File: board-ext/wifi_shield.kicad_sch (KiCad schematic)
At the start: 24 parts, among them J1 Conn_02x05_Counter_Clockwise, J10 Conn_01x01, J11 Conn_01x01, J12 Conn_01x01, J13 Conn_01x01, J14 Conn_01x01, J2 Conn_01x06, J3 Conn_01x04, J4 Conn_01x14, J5 Conn_01x04, J6 Conn_01x14, J7 Conn_01x04, J8 Conn_02x11_Top_Bottom, J9 Conn_01x01, U1 ESP-12E, U2 lowpowerlab_BME280

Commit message: updated design files to kicad7, added GND plane for ext-board v1.3.
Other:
- company: Librelab / SDS / UVA -> librelab

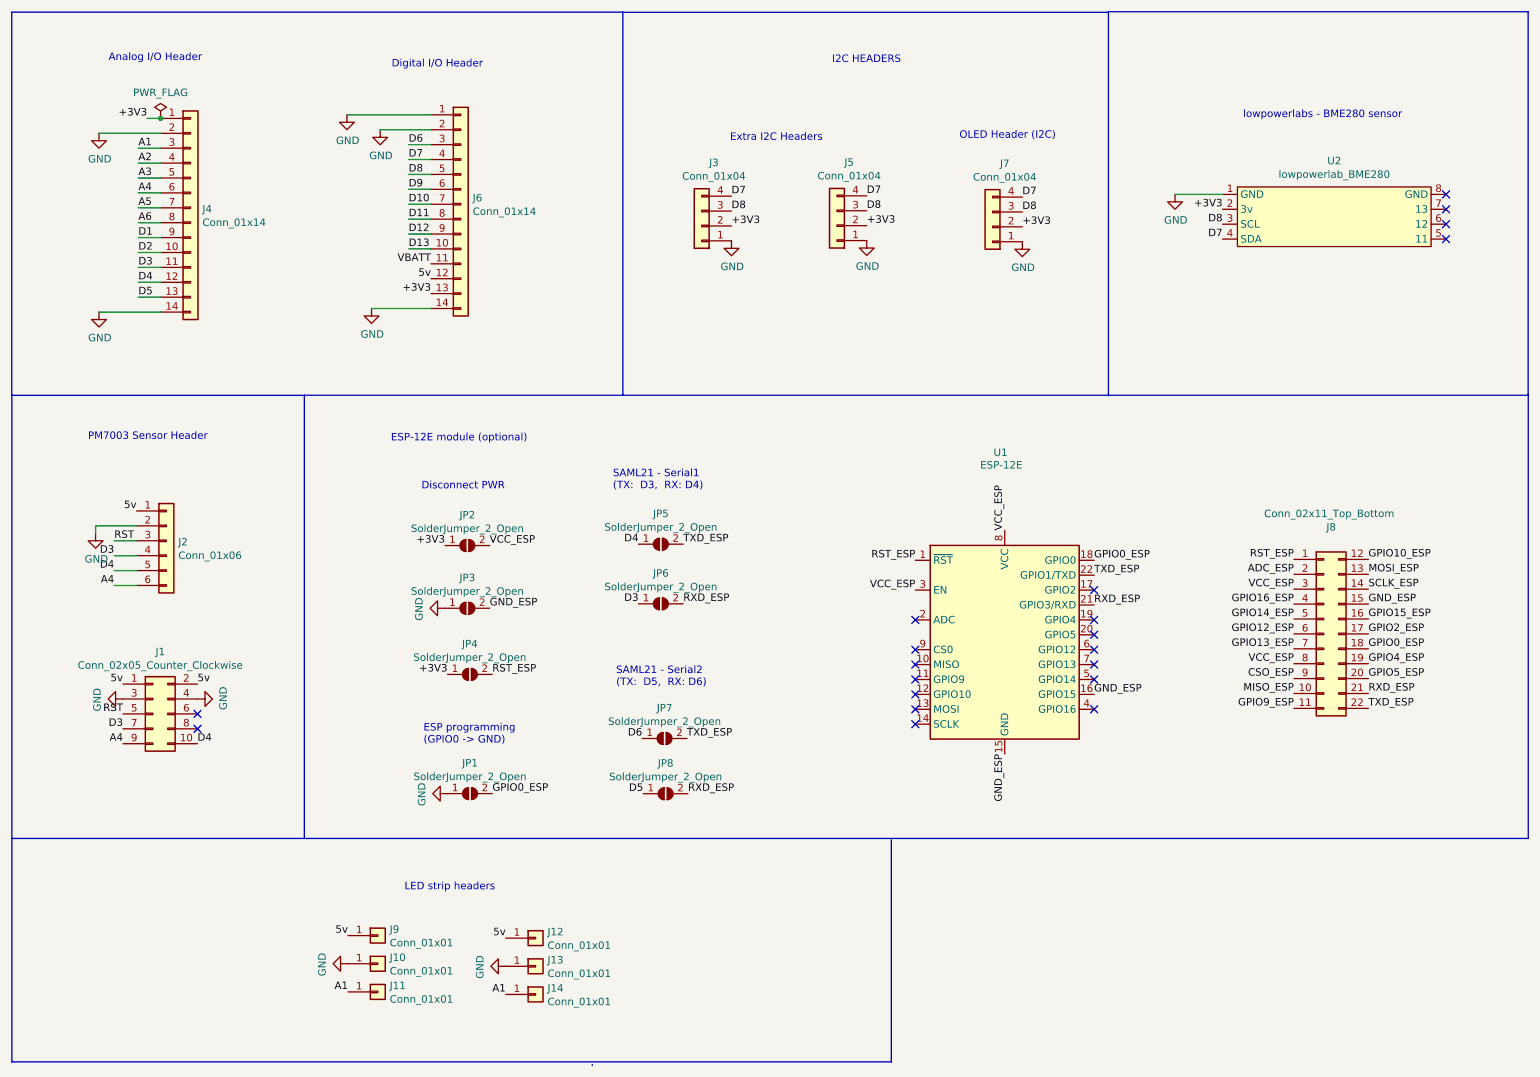
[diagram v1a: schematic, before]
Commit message: added new extension board for Tainã.
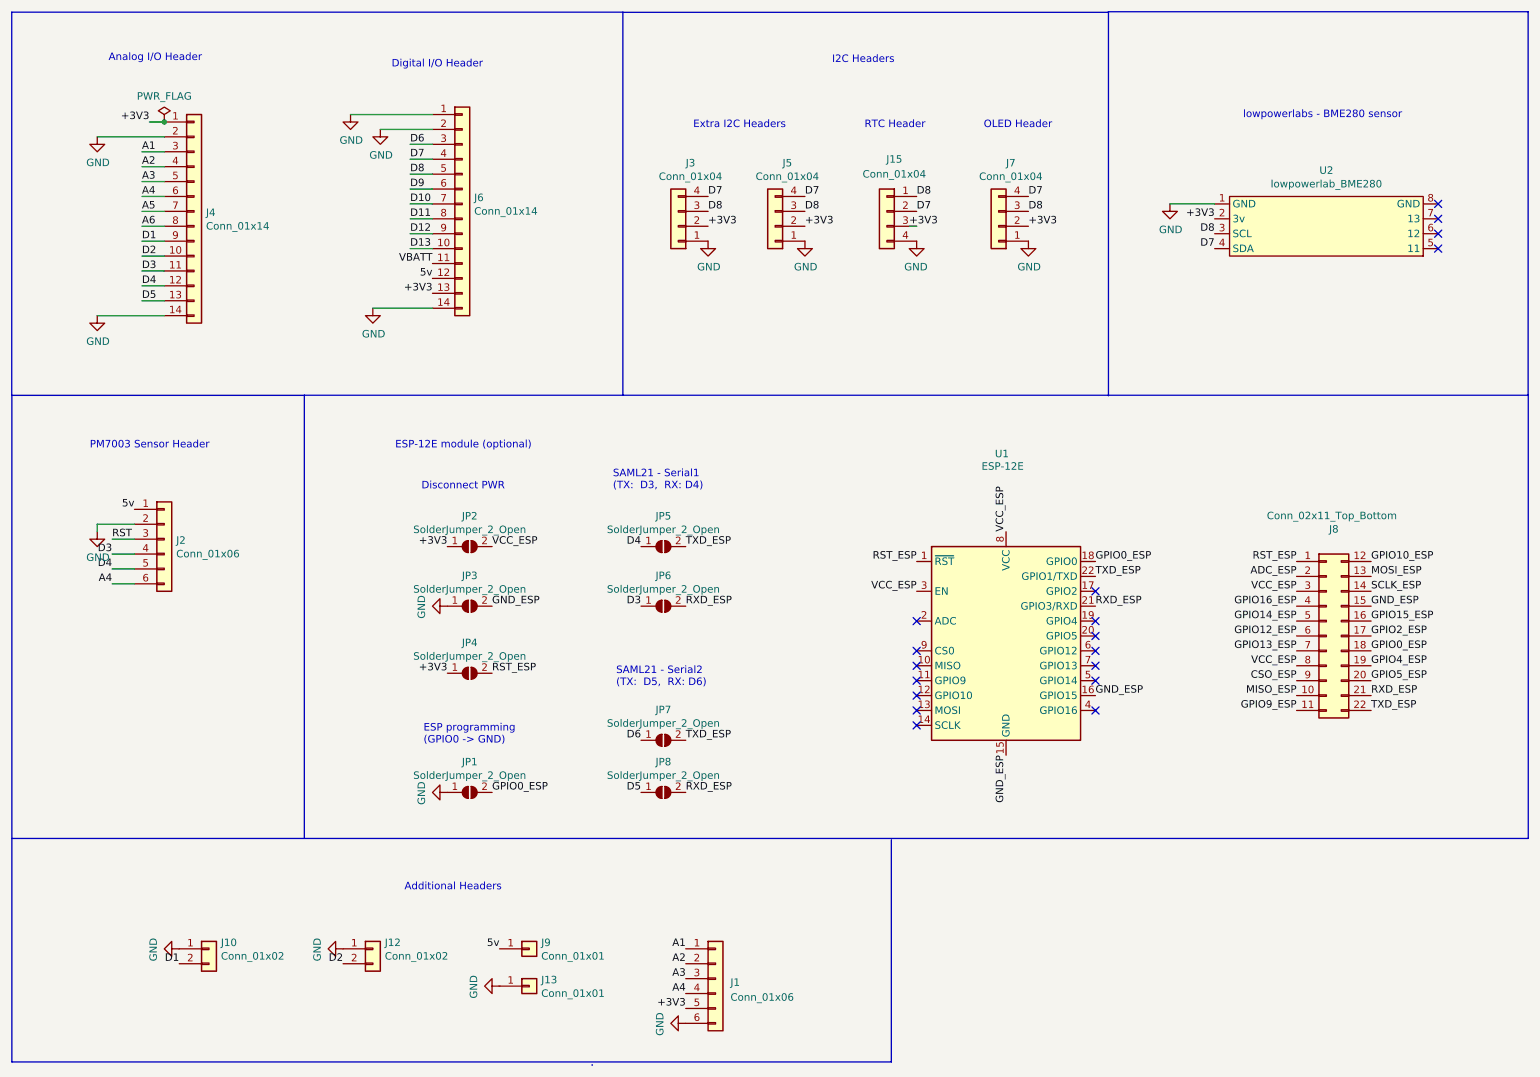
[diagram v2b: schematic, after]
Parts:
- removed J1: Conn_02x05_Counter_Clockwise, Connector_PinHeader_1.27mm:PinHeader_2x05_P1.27mm_Vertical, symbol Connector_Generic:Conn_02x05_Odd_Even
- removed J11, J14: Conn_01x01, Connector_PinHeader_2.54mm:PinHeader_1x01_P2.54mm_Vertical, symbol Connector_Generic:Conn_01x01
- added J1: Conn_01x06, Connector_PinHeader_2.54mm:PinHeader_1x06_P2.54mm_Vertical, symbol Connector_Generic:Conn_01x06
- added J15: Conn_01x04, Connector_PinHeader_2.54mm:PinHeader_1x04_P2.54mm_Vertical, symbol Connector_Generic:Conn_01x04
- J10, J12: value Conn_01x01 -> Conn_01x02; footprint Connector_PinHeader_2.54mm:PinHeader_1x01_P2.54mm_Vertical -> Connector_PinHeader_2.54mm:PinHeader_1x02_P2.54mm_Vertical; symbol Connector_Generic:Conn_01x01 -> Connector_Generic:Conn_01x02
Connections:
- net +3V3: now also J1.5 (Pin_5), J15.3 (Pin_3)
- net 5v: no longer J12.1 (Pin_1)
- net A1: now also J1.1 (Pin_1)
- net A2: now also J1.2 (Pin_2)
- net A3: now also J1.3 (Pin_3)
- net A4: now also J1.4 (Pin_4)
- net D1: now also J10.2 (Pin_2)
- net D2: now also J12.2 (Pin_2)
- net D7: now also J15.2 (Pin_2)
- net D8: now also J15.1 (Pin_1)
- net GND: now also J12.1 (Pin_1), J1.6 (Pin_6), J15.4 (Pin_4)
- no-connect marks 20 -> 18
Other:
- note added: "Additional Headers"
- note added: "I2C Headers"
- note added: "OLED Header"
- note added: "RTC Header"
- note removed: "I2C HEADERS"
- note removed: "LED strip headers"
- note removed: "OLED Header (I2C)"
- moved on the sheet: J13, J3, J4, J5, J7, J8, J9, JP3, JP5, JP6, U2
